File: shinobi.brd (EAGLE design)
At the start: 57 x 47 mm, 112 parts, among them J1 2171790001, J2 61300711121, J3 61301011121, J4 61300211121, J5 61300211121, U1 TV5725, U2 W9864G2JH-6, U3 ESP-06, U4 74ABT125PW, U5 Si5351A-B-GT, U6 CH340C, U7 TPS621351, U8 NCV8187AMN180TAG, Y1 27MHZ 10pF, Y2 25.0MHz 10pF

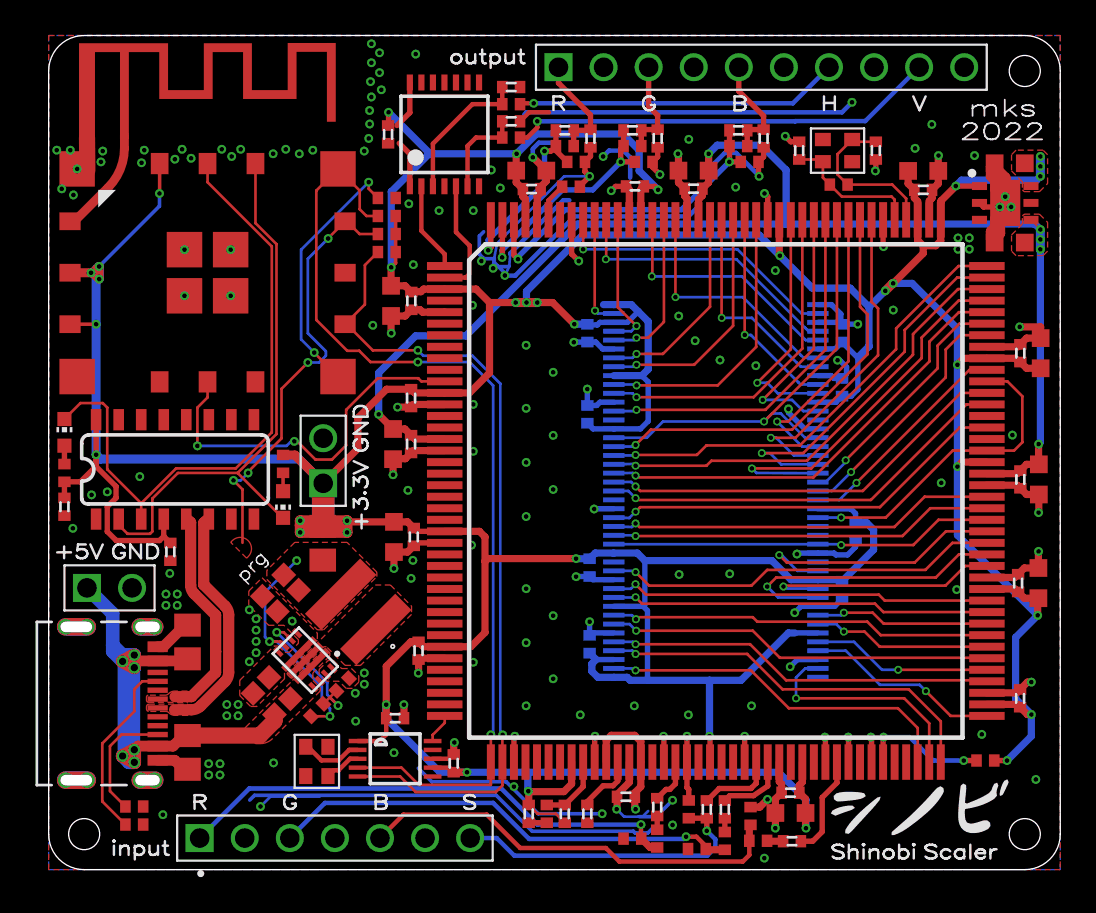
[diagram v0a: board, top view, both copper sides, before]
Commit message: fix gerber issue, update schematic.png
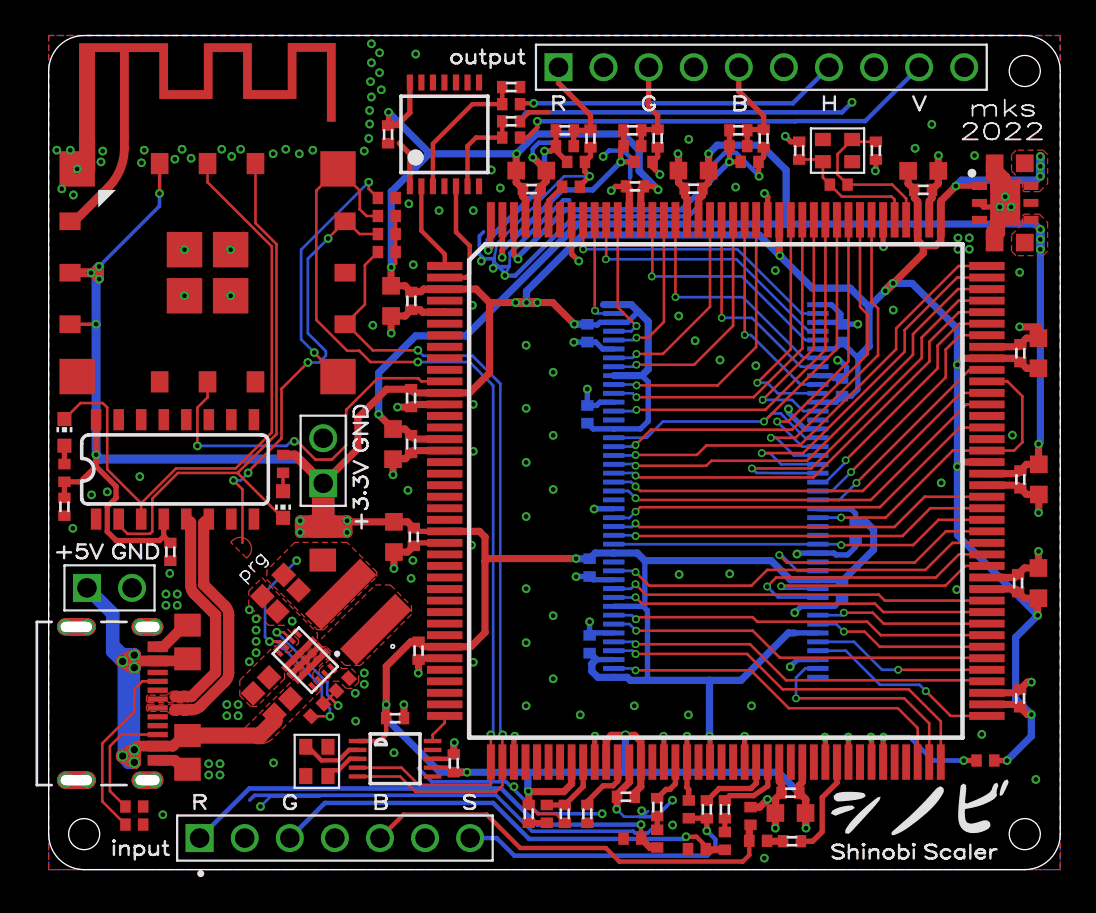
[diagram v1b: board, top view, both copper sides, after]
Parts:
- moved C41 0.13 mm to (55.8, 29.1)
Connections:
- removed net N$21: U2.71
- removed net N$22: U2.59
- net DQM0#: now also U2.71
- net DQM1#: now also U2.59
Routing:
- net +3V3: track 406.8 -> 408.5 mm
- net GND: track 242.3 -> 242.1 mm, vias 178 -> 180

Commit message: update board
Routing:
- net N$61: track 0.00 -> 4.06 mm
- net N$60: track 0.00 -> 4.06 mm
- net N$58: track 0.00 -> 3.56 mm
- net N$50: track 0.00 -> 3.56 mm
- net N$44: track 0.00 -> 3.00 mm
- net N$51: track 0.00 -> 2.64 mm
- net N$59: track 0.00 -> 2.64 mm
- net N$46: track 0.00 -> 2.64 mm
- net N$54: track 0.00 -> 2.64 mm
- net N$53: track 0.00 -> 2.47 mm
- net N$57: track 0.00 -> 2.45 mm
- net N$49: track 0.00 -> 2.45 mm
- net N$45: track 0.00 -> 2.45 mm
- net N$52: track 0.00 -> 1.73 mm
- net N$56: track 0.00 -> 0.82 mm
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
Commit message: update brd
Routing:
- net D+: track 12.0 -> 15.6 mm
- net D-: track 13.2 -> 16.2 mm, vias 0 -> 2
- net N$24: track 6.73 -> 8.18 mm
- net +3V3: track 408.5 -> 409.6 mm
- net N$23: track 10.4 -> 11.4 mm
- net GND: track 242.1 -> 242.2 mm, vias 180 -> 188

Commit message: update with correct ferrite beads
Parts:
- FB1, FB2, FB3: value 10uH -> 220Ω
- renumbered L2 to FB1, L3 to FB2, L4 to FB3
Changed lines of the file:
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@@
 <?xml version="1.0" encoding="utf-8"?>
 <!DOCTYPE eagle SYSTEM "eagle.dtd">
-<eagle version="9.6.1">
+<eagle version="9.6.2">
 <drawing>
 <settings>
@@
 </element>
 <element name="Y2" library="microbuilder" package="CRYSTAL_2.5X2" value="25.0MHz 10pF" x="15.113" y="6.096" smashed="yes" rot="R90"/>
-<element name="L2" library="resistor" library_urn="urn:adsk.eagle:library:2745533" package="R0402" package3d_urn="urn:adsk.eagle:package:2745538/3" value="10uH" x="29.083" y="40.767" smashed="yes"/>
-<element name="L3" library="resistor" library_urn="urn:adsk.eagle:library:2745533" package="R0402" package3d_urn="urn:adsk.eagle:package:2745538/3" value="10uH" x="32.893" y="40.767" smashed="yes"/>
-<element name="L4" library="resistor" library_urn="urn:adsk.eagle:library:2745533" package="R0402" package3d_urn="urn:adsk.eagle:package:2745538/3" value="10uH" x="38.862" y="40.767" smashed="yes"/>
+<element name="FB1" library="resistor" library_urn="urn:adsk.eagle:library:2745533" package="R0402" package3d_urn="urn:adsk.eagle:package:2745538/3" value="220Ω" x="29.083" y="40.767" smashed="yes"/>
+<element name="FB2" library="resistor" library_urn="urn:adsk.eagle:library:2745533" package="R0402" package3d_urn="urn:adsk.eagle:package:2745538/3" value="220Ω" x="32.893" y="40.767" smashed="yes"/>
+<element name="FB3" library="resistor" library_urn="urn:adsk.eagle:library:2745533" package="R0402" package3d_urn="urn:adsk.eagle:package:2745538/3" value="220Ω" x="38.862" y="40.767" smashed="yes"/>
 <element name="C56" library="resistor" library_urn="urn:adsk.eagle:library:2745533" package="C0402" package3d_urn="urn:adsk.eagle:package:2745540/2" value="15pF" x="29.083" y="41.656" smashed="yes"/>
 <element name="C57" library="resistor" library_urn="urn:adsk.eagle:library:2745533" package="C0402" package3d_urn="urn:adsk.eagle:package:2745540/2" value="15pF" x="32.893" y="41.656" smashed="yes"/>
@@
 <contactref element="J3" pad="1"/>
 <contactref element="C56" pad="2"/>
-<contactref element="L2" pad="2"/>
+<contactref element="FB1" pad="2"/>
 <contactref element="C59" pad="1"/>
 <wire x1="30.5308" y1="41.6988" x2="30.488" y2="41.656" width="0.3048" layer="1"/>
@@
 <contactref element="J3" pad="3"/>
 <contactref element="C57" pad="2"/>
-<contactref element="L3" pad="2"/>
+<contactref element="FB2" pad="2"/>
 <contactref element="C60" pad="1"/>
 <wire x1="33.393" y1="40.767" x2="33.393" y2="41.656" width="0.3048" layer="1"/>
@@
 <contactref element="J3" pad="5"/>
 <contactref element="C58" pad="2"/>
-<contactref element="L4" pad="2"/>
+<contactref element="FB3" pad="2"/>
 <contactref element="C61" pad="1"/>
 <wire x1="39.362" y1="41.656" x2="39.362" y2="40.767" width="0.3048" layer="1"/>
@@
 <contactref element="U1" pad="158"/>
 <contactref element="C58" pad="1"/>
-<contactref element="L4" pad="1"/>
+<contactref element="FB3" pad="1"/>
 <contactref element="R16" pad="1"/>
 <via x="38.354" y="39.878" extent="1-16" drill="0.254" diameter="0.508"/>
@@
 <contactref element="U1" pad="159"/>
 <contactref element="C57" pad="1"/>
-<contactref element="L3" pad="1"/>
+<contactref element="FB2" pad="1"/>
 <contactref element="R17" pad="1"/>
 <via x="32.2326" y="39.878" extent="1-16" drill="0.254" diameter="0.508"/>
@@
 <contactref element="U1" pad="160"/>
 <contactref element="C56" pad="1"/>
-<contactref element="L2" pad="1"/>
+<contactref element="FB1" pad="1"/>
 <contactref element="R18" pad="1"/>
 <via x="27.94" y="40.4876" extent="1-16" drill="0.254" diameter="0.508"/>

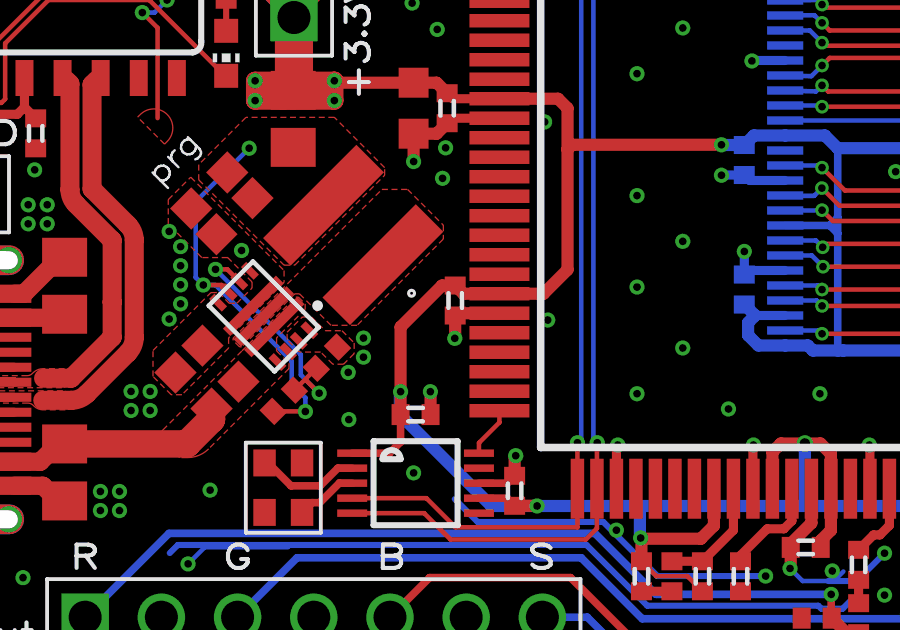
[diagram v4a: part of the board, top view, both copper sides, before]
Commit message: board update
- minor tweak to cap placement (fixes soldermask aperture issue)
-gerbers updated
-iBOM updated
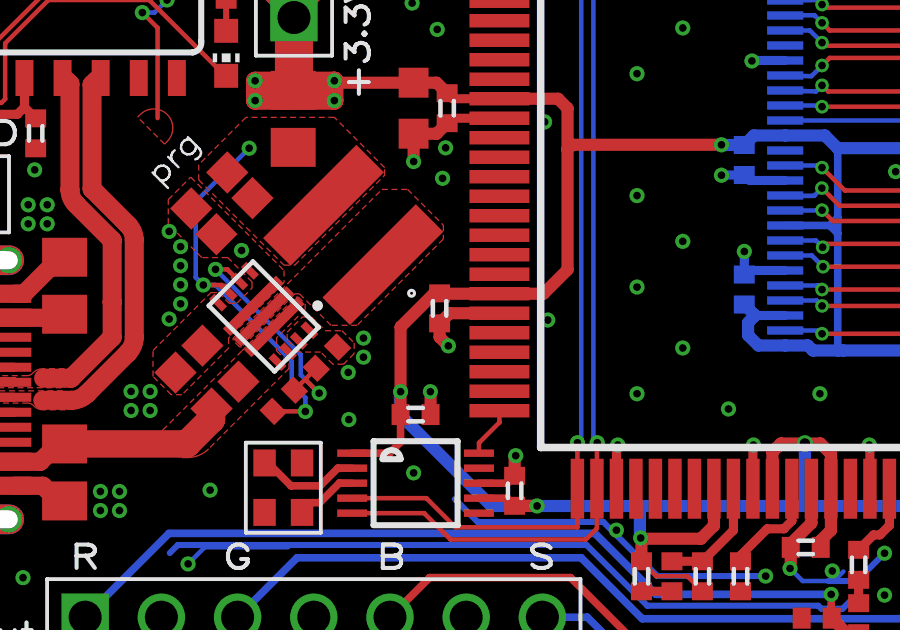
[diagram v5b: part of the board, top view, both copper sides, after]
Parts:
- moved C20 0.58 mm to (20.3, 12.1)
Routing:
- net GND: track 242.2 -> 242.9 mm
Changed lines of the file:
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@@
 <element name="C18" library="resistor" library_urn="urn:adsk.eagle:library:2745533" package="C0603" package3d_urn="urn:adsk.eagle:package:34155559/1" value="10uF" x="36.337" y="39.386" smashed="yes" rot="R180"/>
 <element name="C19" library="resistor" library_urn="urn:adsk.eagle:library:2745533" package="C0603" package3d_urn="urn:adsk.eagle:package:34155559/1" value="10uF" x="55.7934" y="21.987" smashed="yes" rot="R270"/>
-<element name="C20" library="resistor" library_urn="urn:adsk.eagle:library:2745533" package="C0402" package3d_urn="urn:adsk.eagle:package:2745540/2" value="0.1uF" x="20.843" y="12.335" smashed="yes" rot="R270"/>
+<element name="C20" library="resistor" library_urn="urn:adsk.eagle:library:2745533" package="C0402" package3d_urn="urn:adsk.eagle:package:2745540/2" value="0.1uF" x="20.32229375" y="12.07338125" smashed="yes" rot="R270"/>
 <element name="C21" library="resistor" library_urn="urn:adsk.eagle:library:2745533" package="C0402" package3d_urn="urn:adsk.eagle:package:2745540/2" value="0.1uF" x="32.527" y="4.1054" smashed="yes" rot="R180"/>
 <element name="C22" library="resistor" library_urn="urn:adsk.eagle:library:2745533" package="C0402" package3d_urn="urn:adsk.eagle:package:2745540/2" value="0.1uF" x="41.798" y="4.334" smashed="yes" rot="R180"/>
@@
 <wire x1="32.717" y1="4.918" x2="31.9657" y2="4.1667" width="0.4064" layer="1"/>
 <wire x1="32.027" y1="4.1054" x2="31.9657" y2="4.1667" width="0.4064" layer="1"/>
-<wire x1="22.316996875" y1="11.911" x2="20.919" y2="11.911" width="0.4064" layer="1"/>
-<wire x1="20.919" y1="11.911" x2="20.843" y2="11.835" width="0.4064" layer="1"/>
+<wire x1="22.316996875" y1="11.911" x2="20.6599125" y2="11.911" width="0.4064" layer="1"/>
+<wire x1="20.6599125" y1="11.911" x2="20.32229375" y2="11.57338125" width="0.4064" layer="1"/>
 <wire x1="20.421596875" y1="23.4776" x2="20.096996875" y2="23.153" width="0.4064" layer="1"/>
 <wire x1="20.096996875" y1="23.153" x2="19.431003125" y2="23.153" width="0.4064" layer="1"/>
@@
 <wire x1="19.4564" y1="17.8952" x2="19.4564" y2="16.9672" width="0.4064" layer="1"/>
 <via x="19.4564" y="16.9672" extent="1-16" drill="0.254" diameter="0.508"/>
-<wire x1="20.843" y1="11.835" x2="20.843" y2="11.0894" width="0.4064" layer="1"/>
-<wire x1="20.843" y1="11.0894" x2="20.828" y2="11.0744" width="0.4064" layer="1"/>
-<via x="20.828" y="11.0744" extent="1-16" drill="0.254" diameter="0.508"/>
+<wire x1="20.32229375" y1="11.57338125" x2="20.32229375" y2="11.1152875" width="0.4064" layer="1"/>
+<wire x1="20.614640625" y1="10.822940625" x2="20.32229375" y2="11.1152875" width="0.4064" layer="1"/>
+<via x="20.614640625" y="10.822940625" extent="1-16" drill="0.254" diameter="0.508"/>
 <wire x1="20.022" y1="8.532" x2="20.022" y2="9.2896" width="0.4064" layer="1"/>
 <wire x1="20.022" y1="9.2896" x2="20.0152" y2="9.2964" width="0.4064" layer="1"/>
@@
 <wire x1="33.367" y1="4.674" x2="33.027" y2="4.334" width="0.4064" layer="1"/>
 <wire x1="33.027" y1="4.334" x2="33.027" y2="4.1054" width="0.4064" layer="1"/>
-<wire x1="20.974" y1="12.704" x2="20.843" y2="12.835" width="0.4064" layer="1"/>
 <wire x1="42.298" y1="4.334" x2="42.648" y2="3.984" width="0.4064" layer="1"/>
 <wire x1="42.648" y1="3.984" x2="42.648" y2="3.191" width="0.4064" layer="1"/>
@@
 <wire x1="18.6506" y1="7.246" x2="17.4089" y2="7.246" width="0.254" layer="1"/>
 <wire x1="19.022" y1="7.6174" x2="18.6506" y2="7.246" width="0.254" layer="1"/>
-<wire x1="22.317" y1="12.561" x2="21.117" y2="12.561" width="0.4064" layer="1"/>
-<wire x1="21.117" y1="12.561" x2="20.843" y2="12.835" width="0.4064" layer="1"/>
+<wire x1="22.317" y1="12.561" x2="20.334675" y2="12.561" width="0.4064" layer="1"/>
+<wire x1="20.32229375" y1="12.57338125" x2="20.334675" y2="12.561" width="0.4064" layer="1"/>
 <contactref element="U8" pad="1"/>
 <contactref element="U8" pad="6"/>
@@
 <wire x1="23.7878" y1="12.561" x2="22.317" y2="12.561" width="0.4064" layer="1"/>
 <wire x1="24.5872" y1="13.3604" x2="23.7878" y2="12.561" width="0.4064" layer="1"/>
-<wire x1="20.4042" y1="12.835" x2="20.843" y2="12.835" width="0.4064" layer="1"/>
+<wire x1="20.14258125" y1="12.57338125" x2="20.32229375" y2="12.57338125" width="0.4064" layer="1"/>
 <wire x1="19.022" y1="8.532" x2="19.022" y2="9.2964" width="0.4064" layer="1"/>
 <wire x1="19.022" y1="9.2964" x2="19.022" y2="11.4528" width="0.4064" layer="1"/>
-<wire x1="19.022" y1="11.4528" x2="20.4042" y2="12.835" width="0.4064" layer="1"/>
+<wire x1="19.022" y1="11.4528" x2="20.14258125" y2="12.57338125" width="0.4064" layer="1"/>
 <wire x1="52.867" y1="28.811" x2="51.5694" y2="28.811" width="0.4064" layer="1"/>
 <wire x1="51.5694" y1="28.811" x2="51.2064" y2="28.448" width="0.4064" layer="1"/>
